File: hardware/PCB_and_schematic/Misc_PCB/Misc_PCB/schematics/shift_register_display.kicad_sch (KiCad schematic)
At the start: 15 parts, among them J4 LCD_CONN, J6 LCD_DISPLAY, Q8 BC547, U4 74HC595

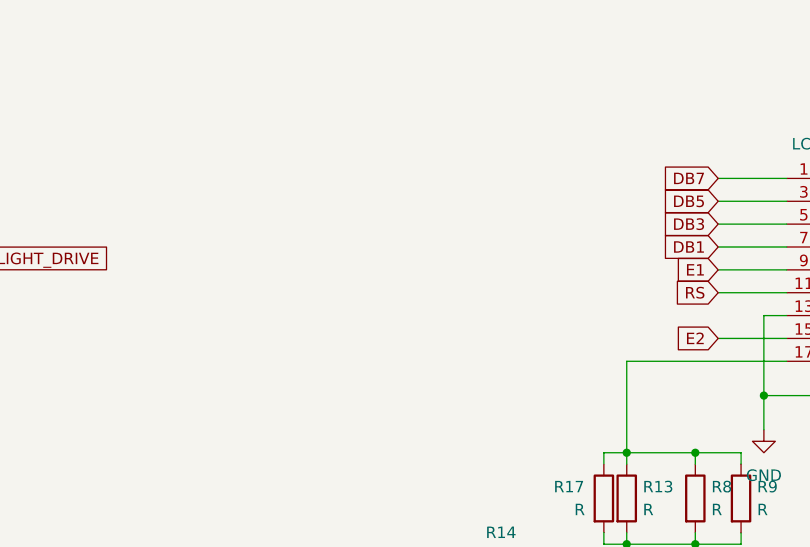
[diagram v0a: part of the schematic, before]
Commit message: Shift register for LCD update
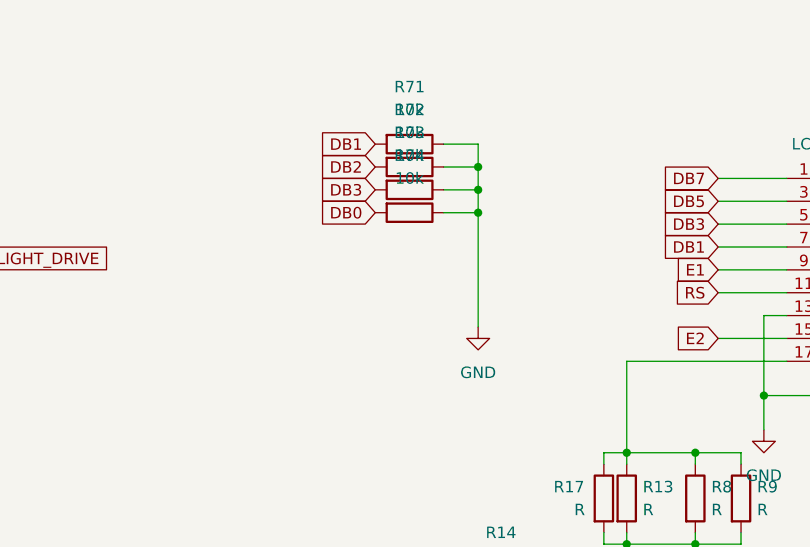
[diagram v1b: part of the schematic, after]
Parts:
- removed C2 (x2): 470u/6,3V, Capacitor_Tantalum_SMD:CP_EIA-3528-21_Kemet-B, symbol Device:C_Polarized
- added C2 (x2): 470u/6,3V, Capacitor_Tantalum_SMD:CP_EIA-3528-21_Kemet-B, symbol Device:C_Polarized
- added R71, R72, R73, R74: 10k, Resistor_SMD:R_0805_2012Metric, symbol Device:R
- Q8: footprint Package_TO_SOT_THT:TO-92_Inline -> My-Footprints:TO-92_Inline_LITTLE_BIGGER
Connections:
- net +5V: now also C2.1, C2.1
- net DB0: now also R74.2
- net DB1: now also R71.2
- net DB2: now also R72.2
- net DB3: now also R73.2
- net GND: now also C2.2, C2.2, R71.1, R72.1, R73.1, R74.1

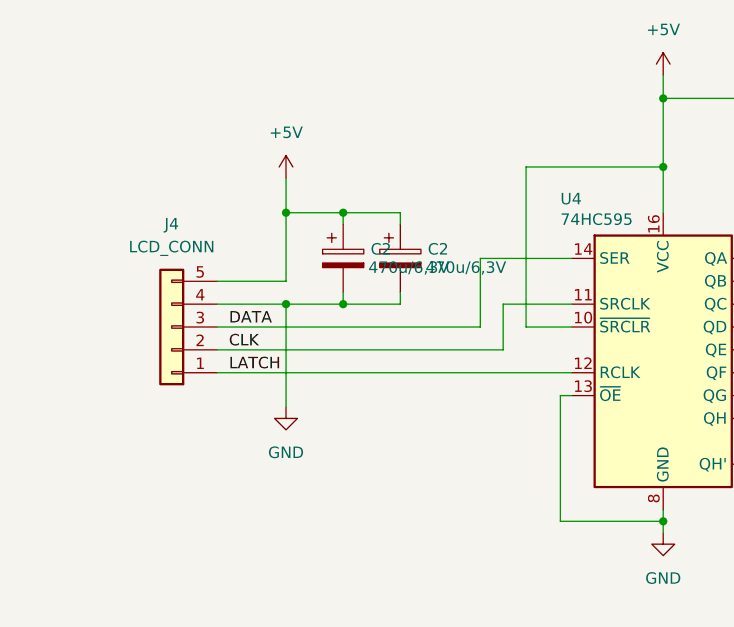
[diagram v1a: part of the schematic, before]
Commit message: add footprint association
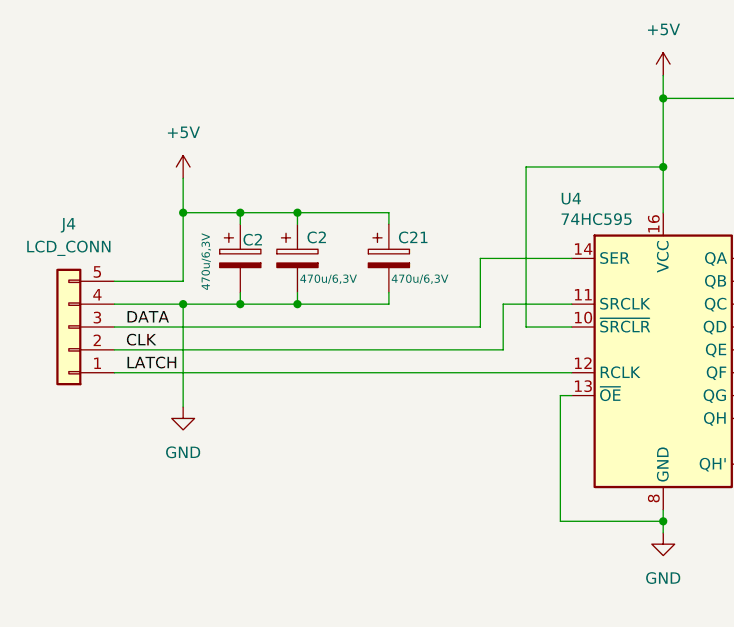
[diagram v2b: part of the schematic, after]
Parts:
- added C21: 470u/6,3V, Capacitor_THT:CP_Radial_D6.3mm_P2.50mm, symbol Device:C_Polarized
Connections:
- net +5V: now also C21.1
- net GND: now also C21.2
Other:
- moved on the sheet: C2, J4

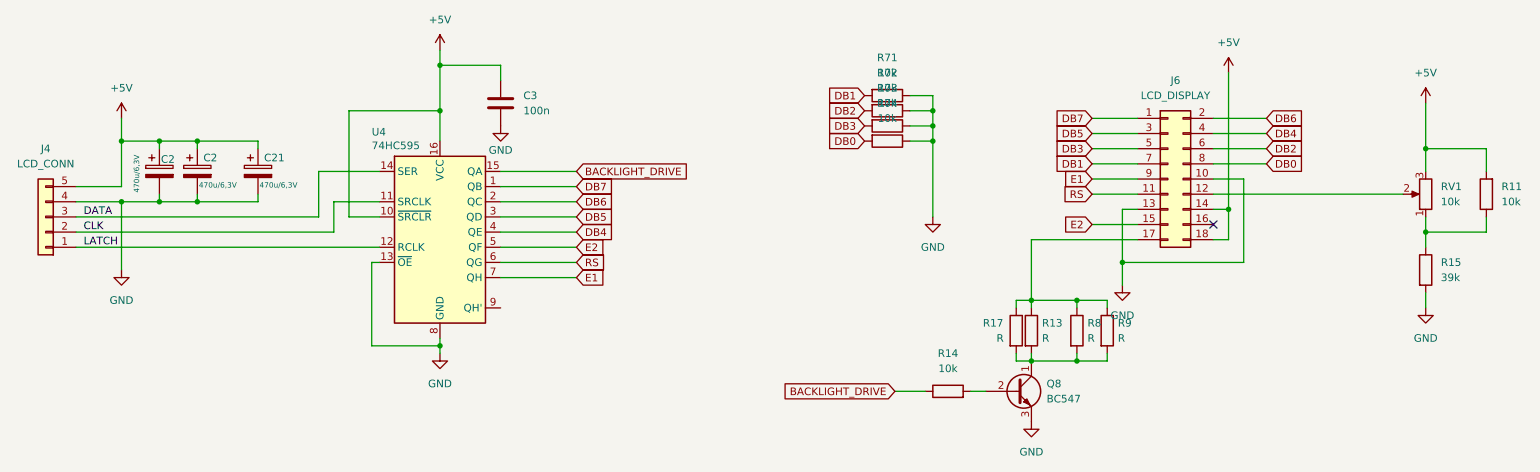
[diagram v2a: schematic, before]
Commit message: update power tracking heater
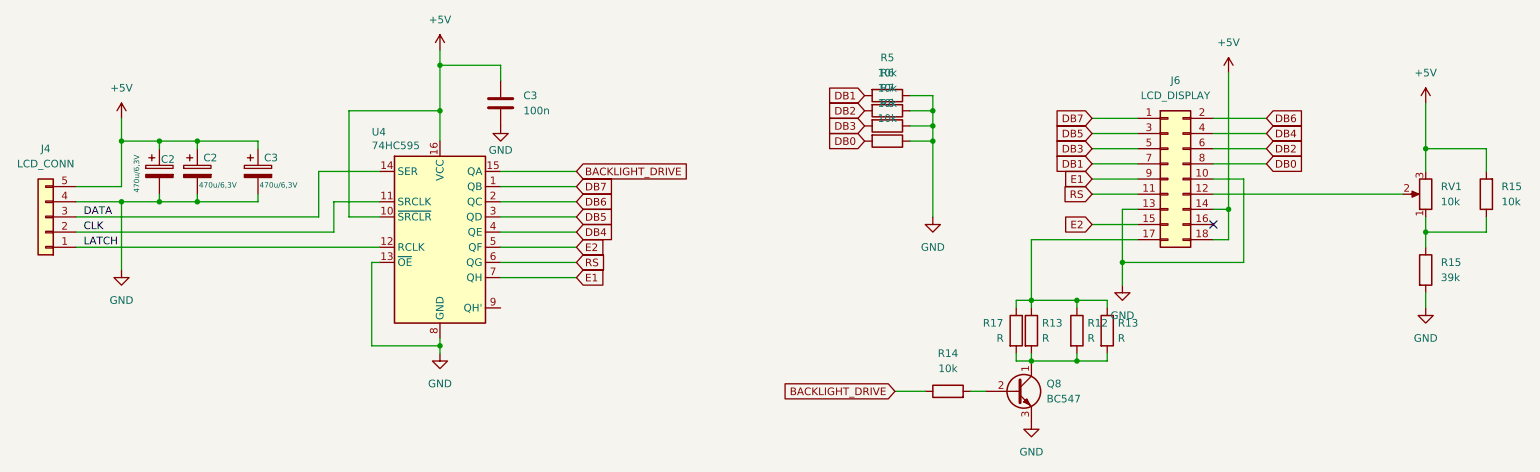
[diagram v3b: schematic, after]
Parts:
- renumbered C21 to C3, R8 to R12, R9 to R13, R11 to R15, R71 to R5, R72 to R6, R73 to R7, R74 to R8
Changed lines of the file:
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@@
 			(project "Misc_PCB"
 				(path "/7b59bc46-701c-4caa-9db8-f0eec290561d/c1486e23-7518-492e-81fc-70742dd392eb"
-					(reference "C3")
+					(reference "C4")
 					(unit 1)
 				)
@@
 		(on_board yes)
 		(dnp no)
-		(property "Reference" "R8"
+		(property "Reference" "R12"
 			(at 192.278 69.85 0)
 			(effects
@@
 			(project "Misc_PCB"
 				(path "/7b59bc46-701c-4caa-9db8-f0eec290561d/c1486e23-7518-492e-81fc-70742dd392eb"
-					(reference "R8")
+					(reference "R12")
 					(unit 1)
 				)
@@
 		(on_board yes)
 		(dnp no)
-		(property "Reference" "C21"
+		(property "Reference" "C3"
 			(at 54.356 42.164 0)
 			(effects
@@
 			(project "Misc_PCB"
 				(path "/7b59bc46-701c-4caa-9db8-f0eec290561d/c1486e23-7518-492e-81fc-70742dd392eb"
-					(reference "C21")
+					(reference "C3")
 					(unit 1)
 				)
@@
 			(project "Misc_PCB"
 				(path "/7b59bc46-701c-4caa-9db8-f0eec290561d/c1486e23-7518-492e-81fc-70742dd392eb"
-					(reference "#PWR017")
+					(reference "#PWR018")
 					(unit 1)
 				)
@@
 		(dnp no)
 		(fields_autoplaced yes)
-		(property "Reference" "R73"
+		(property "Reference" "R7"
 			(at 158.75 30.48 90)
 			(effects
@@
 			(project "Misc_PCB"
 				(path "/7b59bc46-701c-4caa-9db8-f0eec290561d/c1486e23-7518-492e-81fc-70742dd392eb"
-					(reference "R73")
+					(reference "R7")
 					(unit 1)
 				)
@@
 		(on_board yes)
 		(dnp no)
-		(property "Reference" "R9"
+		(property "Reference" "R13"
 			(at 197.358 69.85 0)
 			(effects
@@
 			(project "Misc_PCB"
 				(path "/7b59bc46-701c-4caa-9db8-f0eec290561d/c1486e23-7518-492e-81fc-70742dd392eb"
-					(reference "R9")
+					(reference "R13")
 					(unit 1)
 				)
@@
 			(project "Misc_PCB"
 				(path "/7b59bc46-701c-4caa-9db8-f0eec290561d/c1486e23-7518-492e-81fc-70742dd392eb"
-					(reference "#PWR018")
+					(reference "#PWR019")
 					(unit 1)
 				)
@@
 		(dnp no)
 		(fields_autoplaced yes)
-		(property "Reference" "R74"
+		(property "Reference" "R8"
 			(at 158.75 33.02 90)
 			(effects
@@
 			(project "Misc_PCB"
 				(path "/7b59bc46-701c-4caa-9db8-f0eec290561d/c1486e23-7518-492e-81fc-70742dd392eb"
-					(reference "R74")
+					(reference "R8")
 					(unit 1)
 				)
@@
 			(project "Misc_PCB"
 				(path "/7b59bc46-701c-4caa-9db8-f0eec290561d/c1486e23-7518-492e-81fc-70742dd392eb"
-					(reference "R6")
+					(reference "R10")
 					(unit 1)
 				)
@@
 			(project "Misc_PCB"
 				(path "/7b59bc46-701c-4caa-9db8-f0eec290561d/c1486e23-7518-492e-81fc-70742dd392eb"
-					(reference "R7")
+					(reference "R11")
 					(unit 1)
 				)
@@
 			(project "Misc_PCB"
 				(path "/7b59bc46-701c-4caa-9db8-f0eec290561d/c1486e23-7518-492e-81fc-70742dd392eb"
-					(reference "#PWR021")
+					(reference "#PWR022")
 					(unit 1)
 				)
@@
 			(project "Misc_PCB"
 				(path "/7b59bc46-701c-4caa-9db8-f0eec290561d/c1486e23-7518-492e-81fc-70742dd392eb"
-					(reference "R5")
+					(reference "R9")
 					(unit 1)
 				)
@@
 		(dnp no)
 		(fields_autoplaced yes)
-		(property "Reference" "R72"
+		(property "Reference" "R6"
 			(at 158.75 27.94 90)
 			(effects
@@
 			(project "Misc_PCB"
 				(path "/7b59bc46-701c-4caa-9db8-f0eec290561d/c1486e23-7518-492e-81fc-70742dd392eb"
-					(reference "R72")
+					(reference "R6")
 					(unit 1)
 				)
@@
 		(dnp no)
 		(fields_autoplaced yes)
-		(property "Reference" "#PWR0101"
+		(property "Reference" "#PWR017"
 			(at 166.37 58.42 0)
 			(effects
@@
 			(project "Misc_PCB"
 				(path "/7b59bc46-701c-4caa-9db8-f0eec290561d/c1486e23-7518-492e-81fc-70742dd392eb"
-					(reference "#PWR0101")
+					(reference "#PWR017")
 					(unit 1)
 				)
@@
 			(project "Misc_PCB"
 				(path "/7b59bc46-701c-4caa-9db8-f0eec290561d/c1486e23-7518-492e-81fc-70742dd392eb"
-					(reference "#PWR019")
+					(reference "#PWR020")
 					(unit 1)
 				)
@@
 			(project "Misc_PCB"
 				(path "/7b59bc46-701c-4caa-9db8-f0eec290561d/c1486e23-7518-492e-81fc-70742dd392eb"
-					(reference "R10")
+					(reference "R14")
 					(unit 1)
 				)
@@
 		(dnp no)
 		(fields_autoplaced yes)
-		(property "Reference" "R11"
+		(property "Reference" "R15"
 			(at 261.62 46.9899 0)
 			(effects
@@
 			(project "Misc_PCB"
 				(path "/7b59bc46-701c-4caa-9db8-f0eec290561d/c1486e23-7518-492e-81fc-70742dd392eb"
-					(reference "R11")
+					(reference "R15")
 					(unit 1)
 				)
@@
 			(project "Misc_PCB"
 				(path "/7b59bc46-701c-4caa-9db8-f0eec290561d/c1486e23-7518-492e-81fc-70742dd392eb"
-					(reference "#PWR020")
+					(reference "#PWR021")
 					(unit 1)
 				)
@@
 		(dnp no)
 		(fields_autoplaced yes)
-		(property "Reference" "R71"
+		(property "Reference" "R5"
 			(at 158.75 25.4 90)
 			(effects
@@
 			(project "Misc_PCB"
 				(path "/7b59bc46-701c-4caa-9db8-f0eec290561d/c1486e23-7518-492e-81fc-70742dd392eb"
-					(reference "R71")
-					(unit 1)
-				)
+					(reference "R5")
+					(unit 1)
+				)

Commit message: done LT3652
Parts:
- J6: footprint Connector_PinHeader_2.54mm:PinHeader_2x09_P2.54mm_Vertical -> My-Footprints-connectors:PinHeader_2x09_P2.54mm_Vertical
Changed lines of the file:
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@@
 			)
 		)
-		(property "Footprint" "Connector_PinHeader_2.54mm:PinHeader_2x09_P2.54mm_Vertical"
+		(property "Footprint" "My-Footprints-connectors:PinHeader_2x09_P2.54mm_Vertical"
 			(at 205.74 45.72 0)
 			(effects
